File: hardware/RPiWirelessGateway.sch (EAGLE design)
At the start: 55 parts, among them IC1 MCP1702-3.3, X1 P1A, X2 CONN-SMATHD-SMD-EDGE, X3 P1B, X4 AVR ISP, X5 RPI FTDI

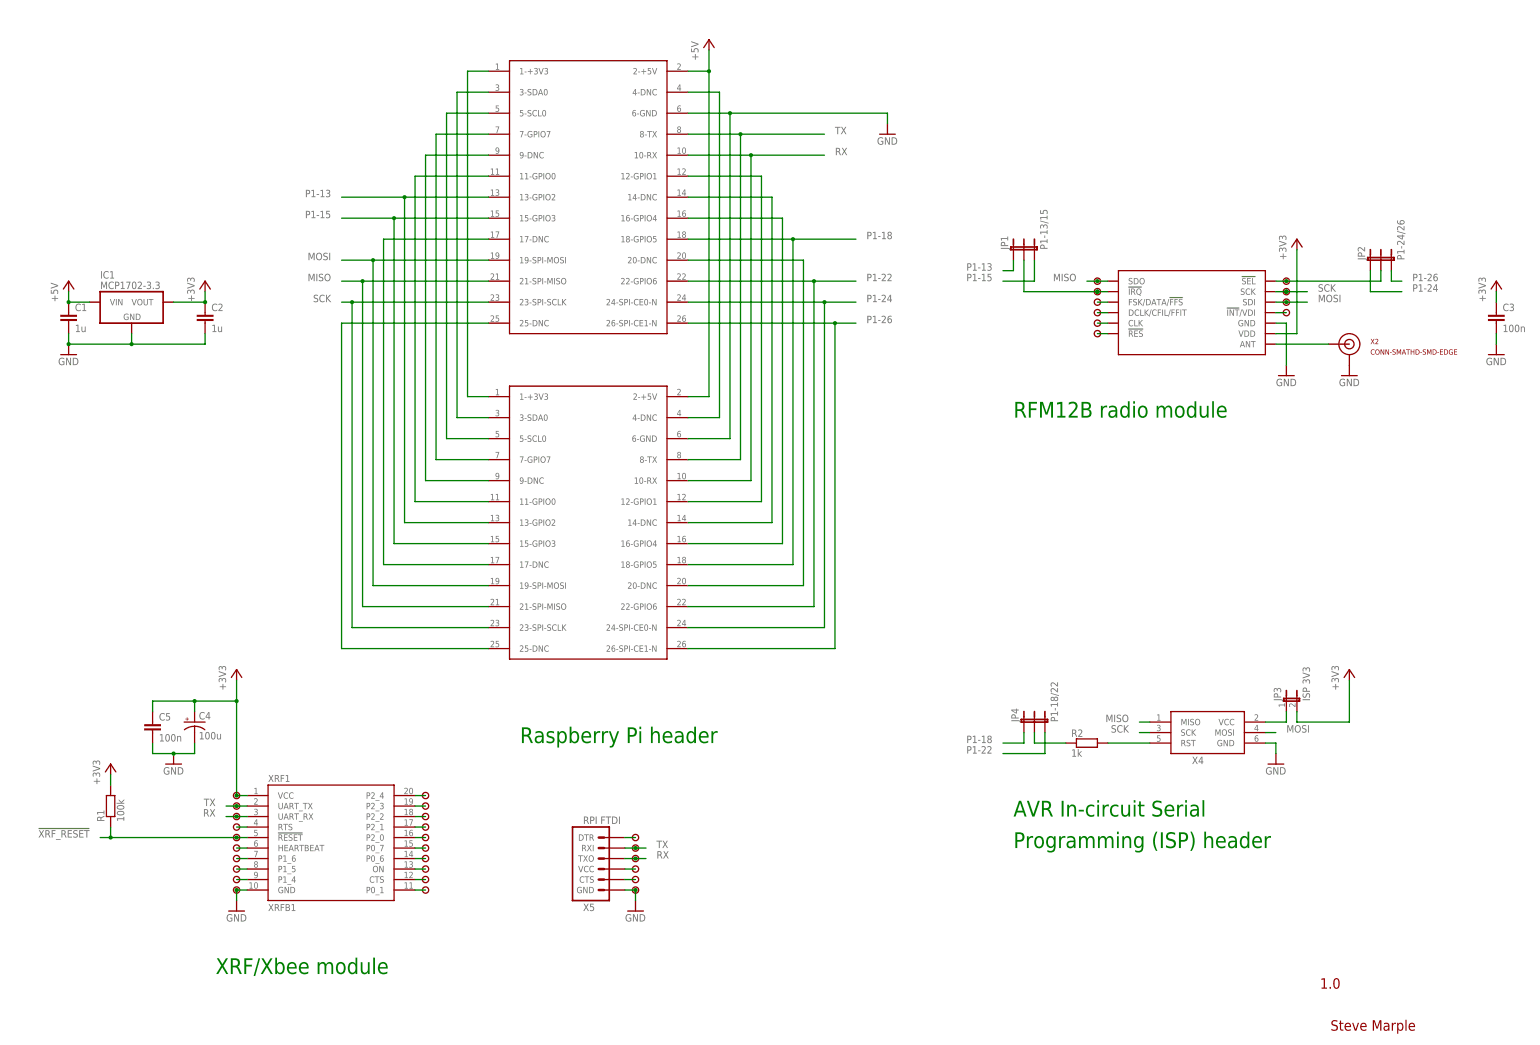
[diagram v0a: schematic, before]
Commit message: Adding resistor to XBee TX line to protect if FTDI also fitted simultaneously.
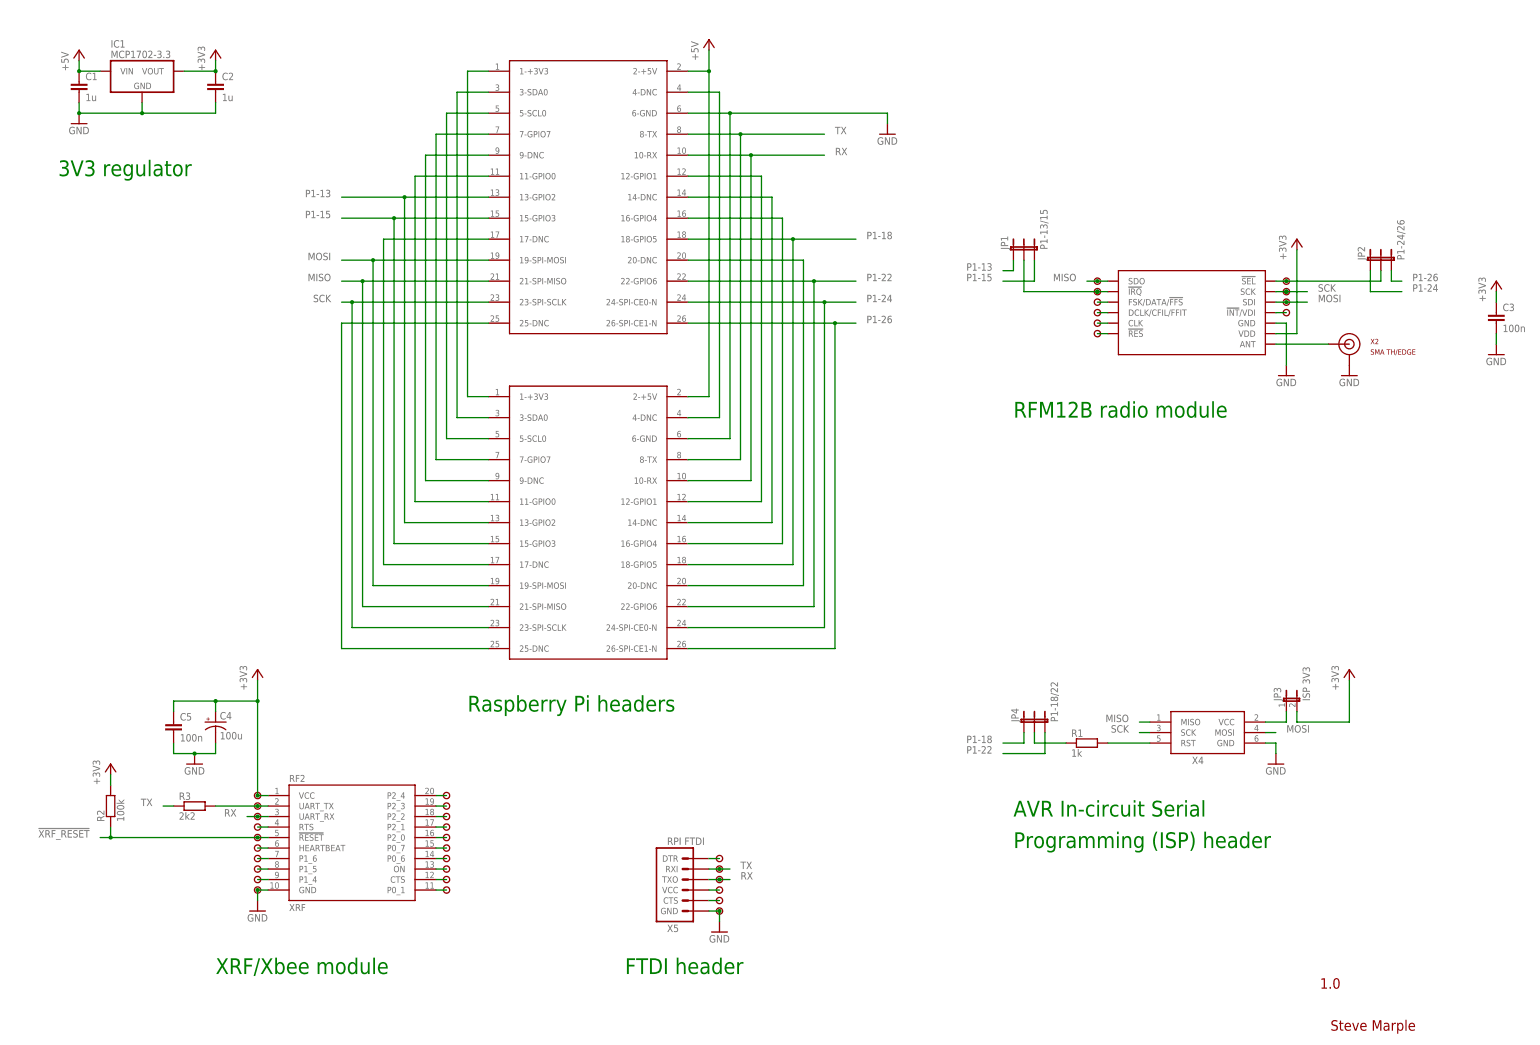
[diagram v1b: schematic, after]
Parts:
- removed XRF1: XRFB1, SteveMarple:XRFB1
- added R3: 2k2, SteveMarple:RESISTOR
- added RF2: XRF, SteveMarple:XRFB1
- R1: value 100k -> 1k
- R2: value 1k -> 100k
- X2: value CONN-SMATHD-SMD-EDGE -> SMA TH/EDGE
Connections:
- new net N$42: R3.2, RF2.UART_TX, U$3.1
- net !XRF_RESET: now also R2.1, RF2.!RESET; no longer R1.1, XRF1.!RESET
- net +3V3: now also R2.2, RF2.VCC; no longer R1.2, XRF1.VCC
- net GND: now also RF2.GND, U$24.1, U$26.1; no longer U$19.1, U$25.1, XRF1.GND
- net N$10: now also RF2.CTS, U$22.1; no longer U$18.1, XRF1.CTS
- net N$11: now also RF2.ON, U$19.1; no longer U$16.1, XRF1.ON
- net N$12: now also RF2.P0_6, U$16.1; no longer U$14.1, XRF1.P0_6
- net N$13: now also RF2.P0_7, U$13.1; no longer U$12.1, XRF1.P0_7
- net N$14: now also RF2.P2_0; no longer XRF1.P2_0
- net N$15: now also RF2.P2_1; no longer XRF1.P2_1
- net N$16: now also RF2.P2_2; no longer XRF1.P2_2
- net N$17: now also RF2.P2_3; no longer XRF1.P2_3
- net N$18: now also RF2.P2_4; no longer XRF1.P2_4
- net N$24: now also R1.2; no longer R2.2
- net N$3: now also RF2.RTS; no longer XRF1.RTS
- net N$30: now also U$23.1; no longer U$24.1
- net N$31: now also U$20.1; no longer U$22.1
- net N$38: now also R1.1; no longer R2.1
- net N$40: now also U$11.1; no longer U$21.1
- net N$5: now also RF2.HEARTBEAT, U$12.1; no longer U$11.1, XRF1.HEARTBEAT
- net N$6: now also RF2.P1_6, U$15.1; no longer U$13.1, XRF1.P1_6
- net N$7: now also RF2.P1_5, U$18.1; no longer U$15.1, XRF1.P1_5
- net N$8: now also RF2.P1_4, U$21.1; no longer U$17.1, XRF1.P1_4
- net N$9: now also RF2.P0_1, U$25.1; no longer U$20.1, XRF1.P0_1
- net RX: now also RF2.UART_RX, U$17.1; no longer U$23.1, XRF1.UART_RX
- net TX: now also R3.1, U$14.1; no longer U$26.1, U$3.1, XRF1.UART_TX
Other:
- note added: "3V3 regulator"
- note added: "FTDI header"
- note added: "Raspberry Pi headers"
- note removed: "Raspberry Pi header"
- moved on the sheet: C1, C2, C4, C5, IC1, R1, R2, X5

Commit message: Adding FET for open-drain control of AVR /RESET
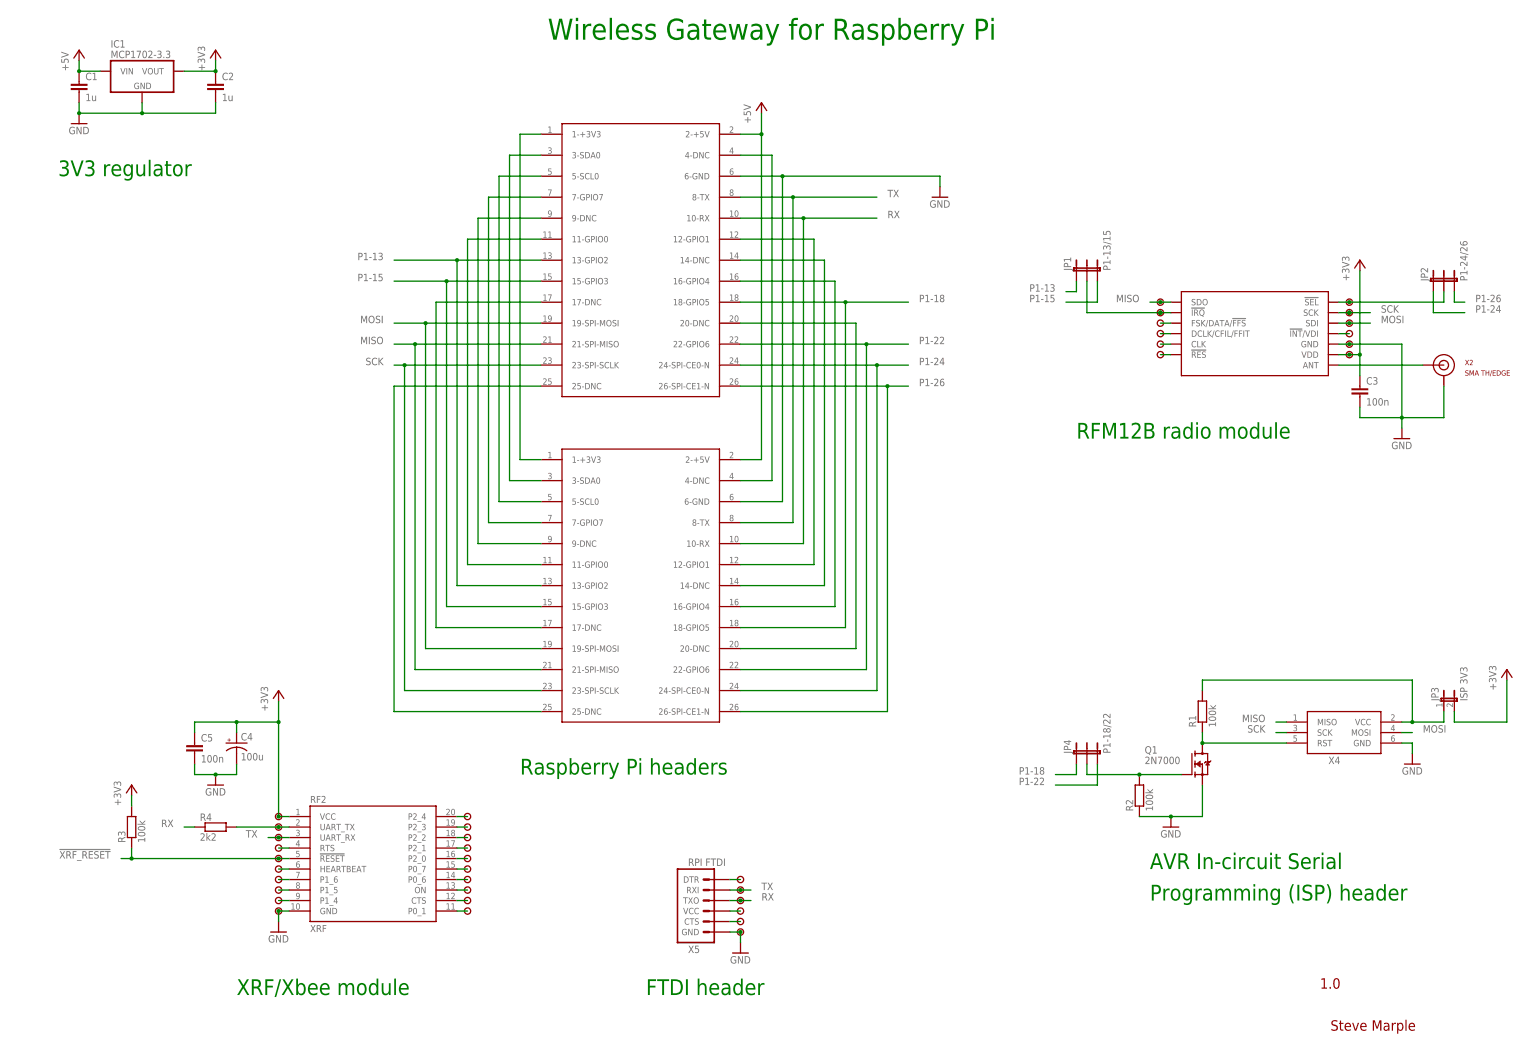
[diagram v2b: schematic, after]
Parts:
- added PAD_RFM12B_!INT!/VDI1, PAD_RFM12B_!INT!/VDI2: PAD, SteveMarple:PAD
- added Q1: 2N7000, SteveMarple:2N7000
- added R4: 2k2, SteveMarple:RESISTOR
- R1: value 1k -> 100k
- R3: value 2k2 -> 100k
- X4: device adafruit:AVRISP-6 -> SteveMarple:AVRISP-HEADER-6-SHROUDED
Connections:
- net !XRF_RESET: now also R3.1; no longer R2.1
- net +3V3: now also PAD_RFM12B_!INT!/VDI2.1, R3.2; no longer R2.2
- net GND: now also PAD_RFM12B_!INT!/VDI1.1, Q1.S, R2.1, U$22.1; no longer U$24.1
- net N$10: now also U$20.1; no longer U$22.1
- net N$11: now also U$17.1; no longer U$19.1
- net N$12: now also U$14.1; no longer U$16.1
- net N$13: now also U$12.1; no longer U$13.1
- net N$24: now also Q1.D, R1.1; no longer R1.2
- net N$30: now also U$25.1; no longer U$23.1
- net N$31: now also U$24.1; no longer U$20.1
- net N$38: now also Q1.G, R2.2; no longer R1.1
- net N$4: now also R1.2
- net N$40: now also U$15.1; no longer U$11.1
- net N$42: now also R4.2; no longer R3.2
- net N$5: now also U$11.1; no longer U$12.1
- net N$6: now also U$13.1; no longer U$15.1
- net N$7: now also U$16.1; no longer U$18.1
- net N$8: now also U$19.1; no longer U$21.1
- net N$9: now also U$23.1; no longer U$25.1
- net RX: now also R4.1, U$21.1; no longer RF2.UART_RX, U$17.1, U$5.1
- net TX: now also RF2.UART_RX, U$18.1, U$5.1; no longer R3.1, U$14.1
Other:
- note added: "Wireless Gateway for Raspberry Pi"
- moved on the sheet: C3, C4, C5, JP1, JP2, JP3, JP4, R1, R2, R3, RF2, X2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

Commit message: Added optional pull-up for /FFS. Move breakout pads for XRF/XBee to allow Sparkfun XBee breakout board to be fitted.
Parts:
- added R5: 2k2, SteveMarple:RESISTOR
- R4: value 2k2 -> 100k
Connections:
- net !XRF_RESET: now also R4.1; no longer R3.1
- net +3V3: now also R1.2, R4.2; no longer R3.2
- net GND: now also R3.1; no longer R2.1
- net N$20: now also R1.1
- net N$24: now also R2.1; no longer R1.1
- net N$38: now also R3.2; no longer R2.2
- net N$4: now also R2.2; no longer R1.2
- net N$42: now also R5.2; no longer R4.2
- net RX: now also R5.1; no longer R4.1
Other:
- moved on the sheet: JP1, R1, R2, R3, R4

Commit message: Removed pullup for /FFS (internal pullup present). New RFM12B footprint.
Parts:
- removed R5: 2k2, SteveMarple:RESISTOR
- R4: value 100k -> 2k2
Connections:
- net !XRF_RESET: now also R3.1; no longer R4.1
- net +3V3: now also R3.2; no longer R1.2, R4.2
- net GND: now also R2.1; no longer R3.1
- net N$20: no longer R1.1
- net N$24: now also R1.1; no longer R2.1
- net N$38: now also R2.2; no longer R3.2
- net N$4: now also R1.2; no longer R2.2
- net N$42: now also R4.2; no longer R5.2
- net RX: now also R4.1; no longer R5.1
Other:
- moved on the sheet: R1, R2, R3, R4
